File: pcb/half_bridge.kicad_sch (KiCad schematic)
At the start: 15 parts, among them Q1 IKW40N120H3, Q2 IKW40N120H3, U1 UCC21550BDWK

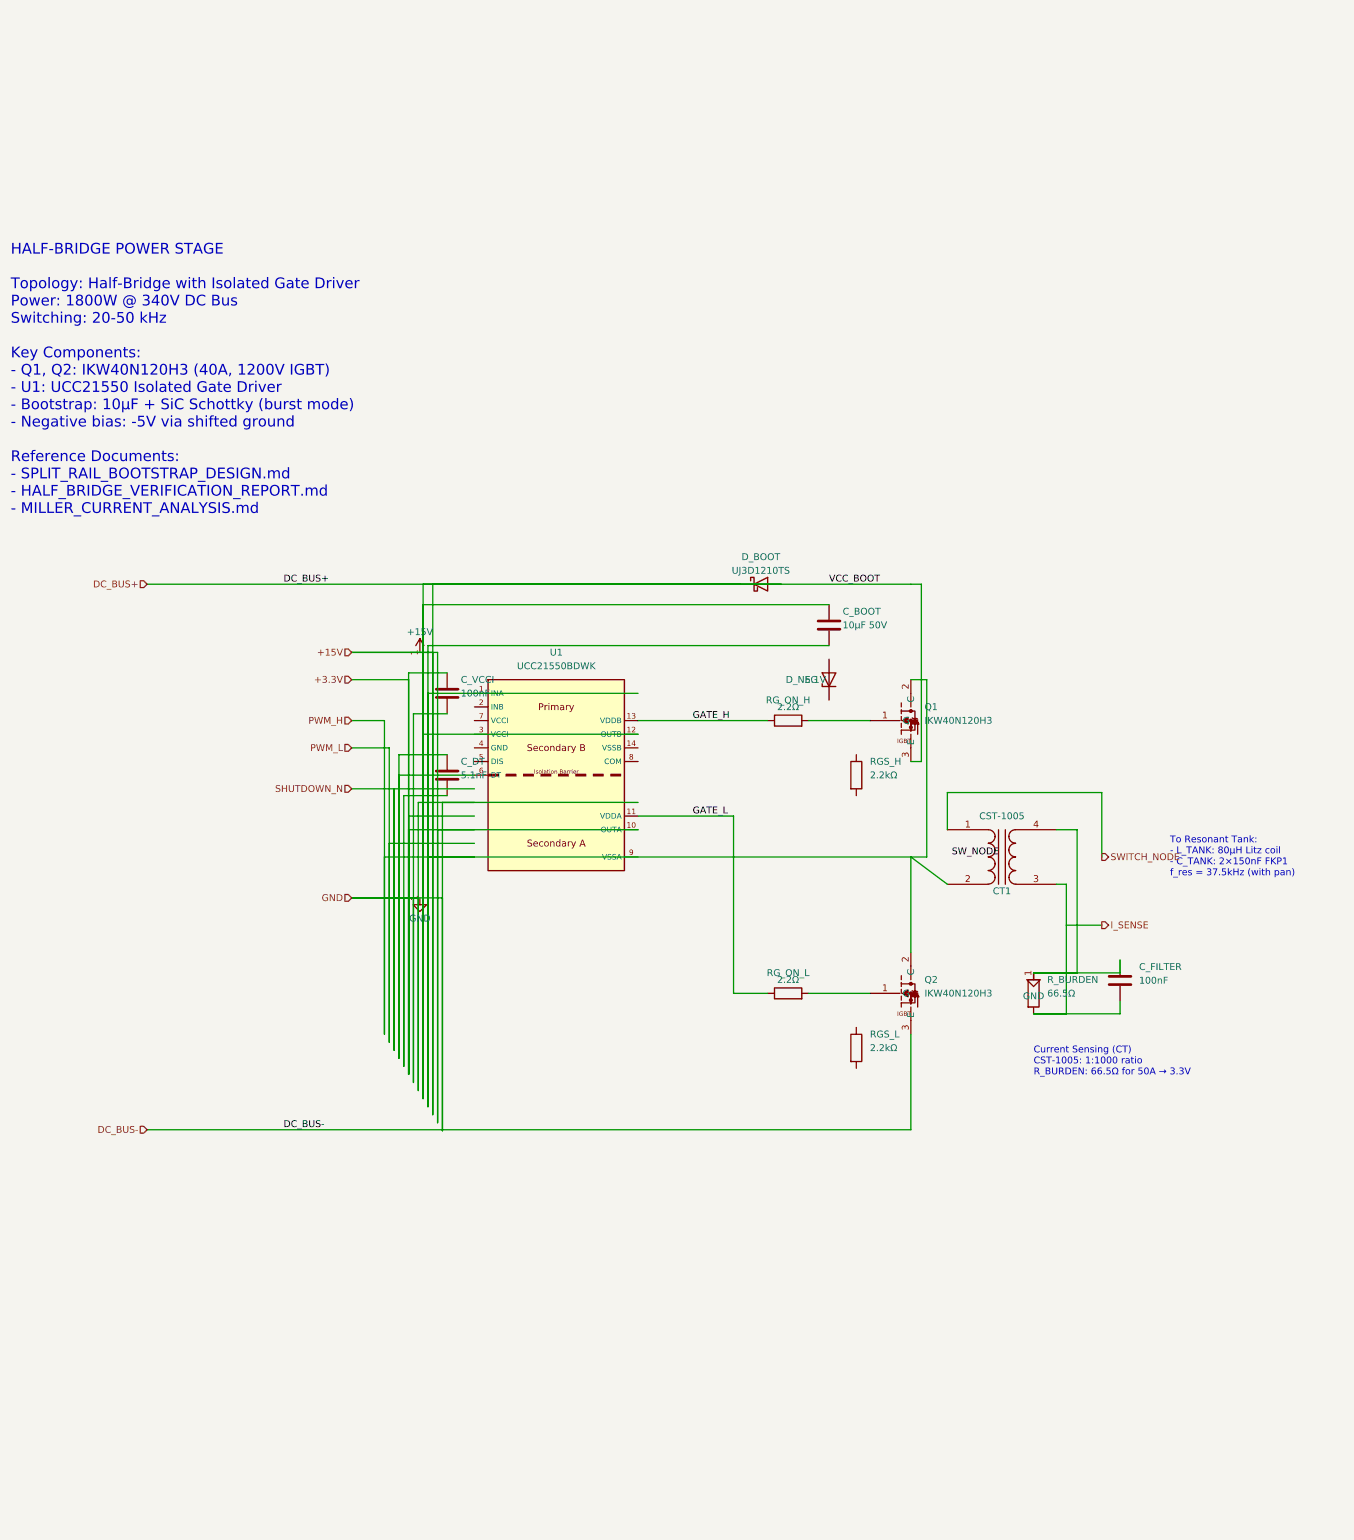
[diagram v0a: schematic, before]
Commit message: feat: generate KiCad schematics from atopile netlist
scripts/gen_schematics.py generates all 7 hierarchical KiCad schematic
files (root + 6 sub-sheets) from elec/build/default.net:

- Synthesizes box symbols from netlist libpart pin counts
- Pure label-per-pin connectivity (no wires)
- Hierarchical labels for inter-sheet nets
- Deterministic UUIDs from atopile tstamps
- Built-in oracle verifies connectivity partition isomorphism
- No-connect markers on intentionally-unconnected pins

Oracle: ORACLE PASS — 346 pin assignments, 73 multi-node nets,
connectivity partitions isomorphic.

Integrated into Makefile via 'make schematics' target.
Manifest entry added per repo convention.
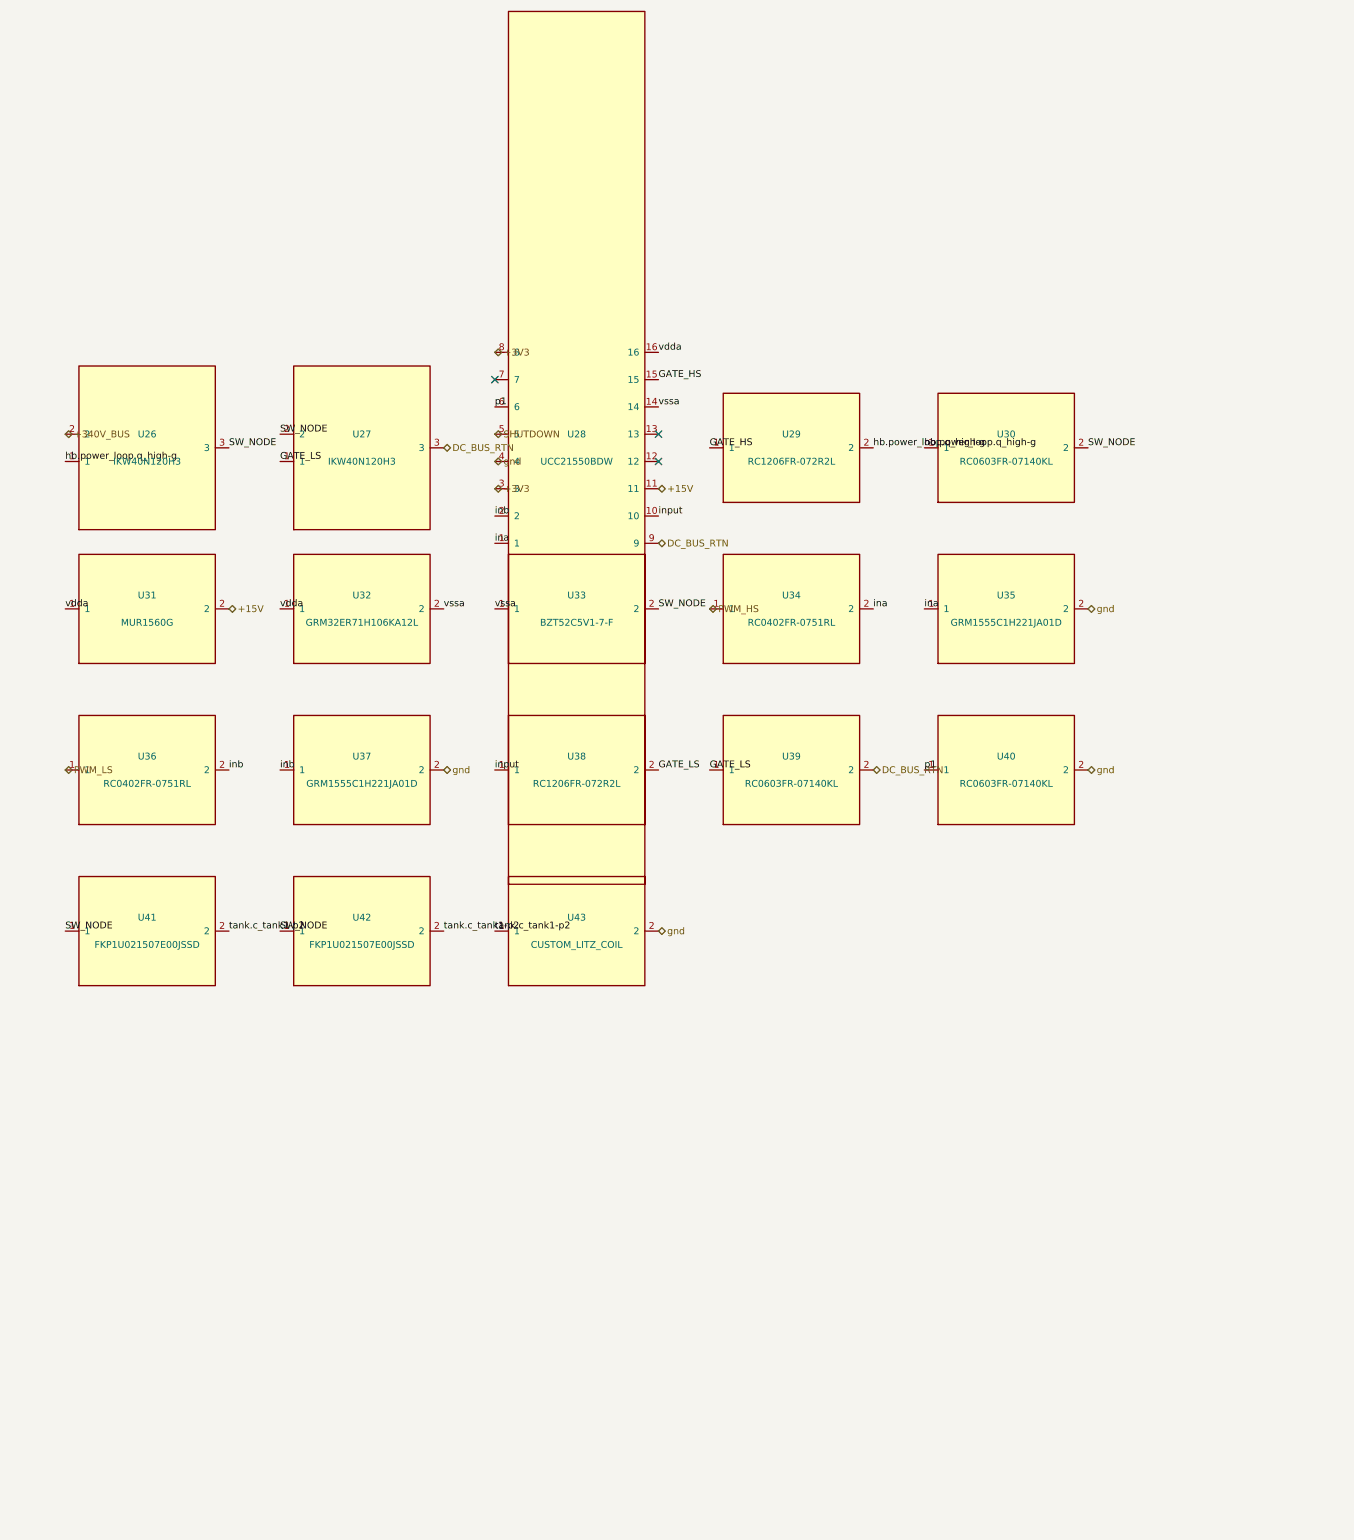
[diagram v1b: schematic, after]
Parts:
- removed CT1: CST-1005, temper:CST-1005, symbol Device:Transformer_1P_1S
- removed C_BOOT: 10µF 50V, Capacitor_SMD:C_1210_3225Metric, symbol Device:C
- removed C_DT: 5.1nF, Capacitor_SMD:C_0603_1608Metric, symbol Device:C
- removed C_FILTER, C_VCCI: 100nF, Capacitor_SMD:C_0603_1608Metric, symbol Device:C
- removed D_BOOT: UJ3D1210TS, Package_TO_SOT_THT:TO-220-2_Vertical, symbol Device:D_Schottky
- removed D_NEG: 5.1V, Diode_SMD:D_SOD-123, symbol Device:D_Zener
- removed Q1, Q2: IKW40N120H3, Package_TO_SOT_THT:TO-247-3_Vertical, symbol IKW40N120H3:IKW40N120H3
- removed RGS_H, RGS_L: 2.2kΩ, Resistor_SMD:R_0603_1608Metric, symbol Device:R
- removed RG_ON_H, RG_ON_L: 2.2Ω, Resistor_SMD:R_1206_3216Metric, symbol Device:R
- removed R_BURDEN: 66.5Ω, Resistor_SMD:R_1206_3216Metric, symbol Device:R
- removed U1: UCC21550BDWK, Package_SO:SOIC-16W_7.5x10.3mm_P1.27mm, symbol UCC21550:UCC21550DWK
- added U26, U27: IKW40N120H3, Package_TO_SOT_THT:TO-247-3_Vertical, symbol IKW40N120H3
- added U28: UCC21550BDW, lib:SOIC16W_Isolated, symbol UCC21550BDW
- added U29, U38: RC1206FR-072R2L, Resistor_SMD:R_1206_3216Metric, symbol RC1206FR-072R2L
- added U30, U39, U40: RC0603FR-07140KL, Resistor_SMD:R_0603_1608Metric, symbol RC0603FR-07140KL
- added U31: MUR1560G, Package_TO_SOT_THT:TO-220-2_Vertical, symbol MUR1560G
- added U32: GRM32ER71H106KA12L, Capacitor_SMD:C_1210_3225Metric, symbol GRM32ER71H106KA12L
- added U33: BZT52C5V1-7-F, Diode_SMD:D_SOD-123, symbol BZT52C5V1-7-F
- added U34, U36: RC0402FR-0751RL, Resistor_SMD:R_0402_1005Metric, symbol RC0402FR-0751RL
- added U35, U37: GRM1555C1H221JA01D, Capacitor_SMD:C_0402_1005Metric, symbol GRM1555C1H221JA01D
- added U41, U42: FKP1U021507E00JSSD, Capacitor_THT:C_Rect_L31.5mm_W13.0mm_P27.50mm_MKS4, symbol FKP1U021507E00JSSD
- added U43: CUSTOM_LITZ_COIL, lib:LitzPad_15A, symbol CUSTOM_LITZ_COIL
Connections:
- net +15V: now also U28.11, U31.2
- net SW_NODE: now also U26.3, U27.2, U30.2, U33.2, U41.1, U42.1
- new net +340V_BUS: U26.2
- new net +3V3: U28.3, U28.8
- new net DC_BUS_RTN: U27.3, U28.9, U39.2
- new net GATE_HS: U28.15, U29.1
- new net GATE_LS: U27.1, U38.2, U39.1
- new net PWM_HS: U34.1
- new net PWM_LS: U36.1
- new net SHUTDOWN: U28.5
- new net gnd: U28.4, U35.2, U37.2, U40.2, U43.2
- new net hb.power_loop.q_high-g: U26.1, U29.2, U30.1
- new net ina: U28.1, U34.2, U35.1
- new net inb: U28.2, U36.2, U37.1
- new net input: U28.10, U38.1
- new net p1: U28.6, U40.1
- new net tank.c_tank1-p2: U41.2, U42.2, U43.1
- new net vdda: U28.16, U31.1, U32.1
- new net vssa: U28.14, U32.2, U33.1
- no-connect marks 0 -> 3
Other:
- note removed: "Current Sensing (CT) CST-1005: 1:1000 ratio R_BURDEN: 66.5Ω for 50A → 3.3V"
- note removed: "HALF-BRIDGE POWER STAGE Topology: Half-Bridge with Isolated Gate Driver Power: 1800W @ 340V DC Bus Switching: 20-50 kHz Key Components: - Q1, Q2: IKW40N120H3 (40A, 1200V IGBT) - U1: UCC21550 Isolated Gate Driver - Bootstrap: 10µF + SiC Schottky (burst mode) - Negative bias: -5V via shifted ground Reference Documents: - SPLIT_RAIL_BOOTSTRAP_DESIGN.md - HALF_BRIDGE_VERIFICATION_REPORT.md - MILLER_C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"
- note removed: "To Resonant Tank: - L_TANK: 80µH Litz coil - C_TANK: 2×150nF FKP1 f_res = 37.5kHz (with pan)"
- title: Half Bridge Power Stage -> Half_Bridge

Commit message: chore: regenerate schematics from atopile netlist (#228)
Generated from elec/build/default.net via gen_schematics.py.
Adds 23 new components from discharge (17), aux_supply (4), and
thermal (2) modules that were previously un-mapped and absent.
Root sheet layout re-stacked with dynamic spacing.
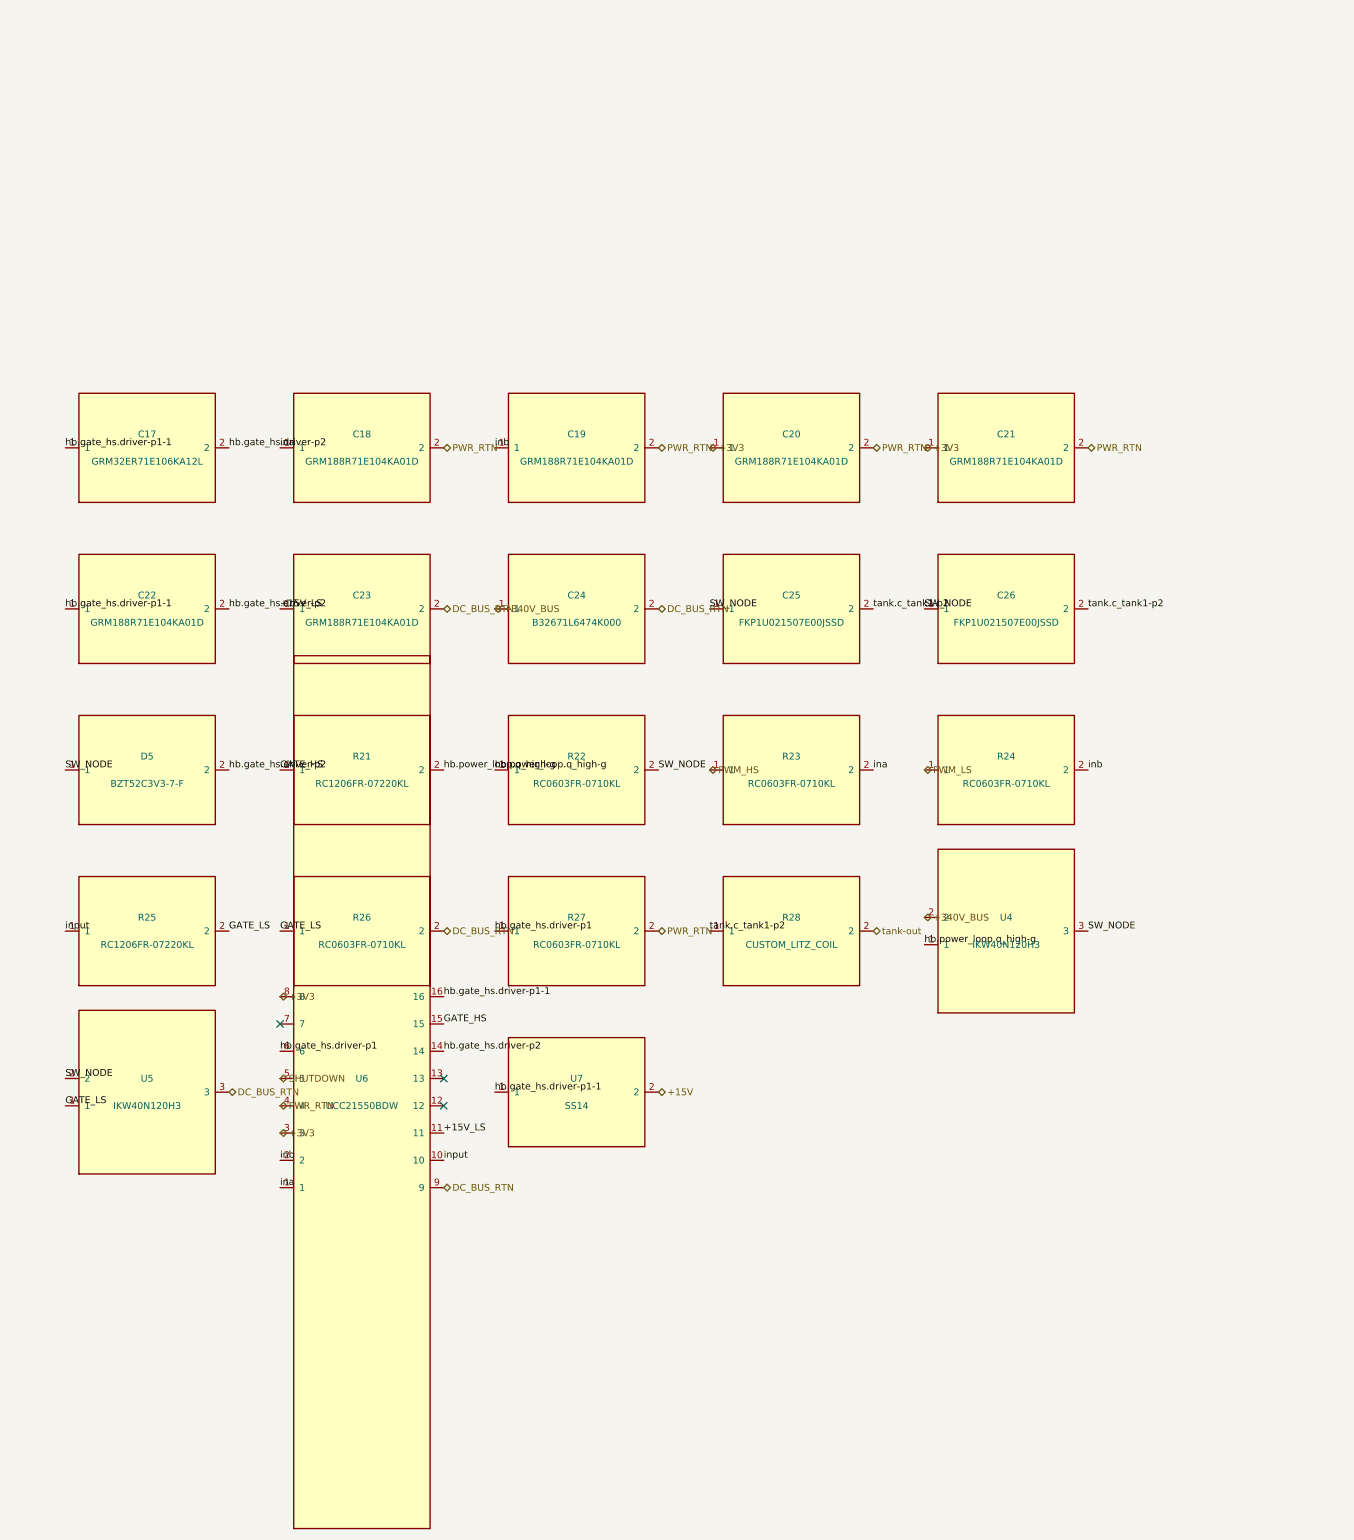
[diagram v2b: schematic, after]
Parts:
- added C20, C21, C22, C23: GRM188R71E104KA01D, Capacitor_SMD:C_0603_1608Metric, symbol GRM188R71E104KA01D
- added C24: B32671L6474K000, Capacitor_THT:C_Rect_L18.0mm_W11.0mm_P15.00mm_FKS3_FKP3, symbol B32671L6474K000
- C17: renamed from U32; value GRM32ER71H106KA12L -> GRM32ER71E106KA12L; symbol GRM32ER71H106KA12L -> GRM32ER71E106KA12L
- C18: renamed from U35; value GRM1555C1H221JA01D -> GRM188R71E104KA01D; footprint Capacitor_SMD:C_0402_1005Metric -> Capacitor_SMD:C_0603_1608Metric; symbol GRM1555C1H221JA01D -> GRM188R71E104KA01D
- C19: renamed from U37; value GRM1555C1H221JA01D -> GRM188R71E104KA01D; footprint Capacitor_SMD:C_0402_1005Metric -> Capacitor_SMD:C_0603_1608Metric; symbol GRM1555C1H221JA01D -> GRM188R71E104KA01D
- D5: renamed from U33; value BZT52C5V1-7-F -> BZT52C3V3-7-F; symbol BZT52C5V1-7-F -> BZT52C3V3-7-F
- R21: renamed from U29; value RC1206FR-072R2L -> RC1206FR-07220KL; symbol RC1206FR-072R2L -> RC1206FR-07220KL
- R22: renamed from U30; value RC0603FR-07140KL -> RC0603FR-0710KL; symbol RC0603FR-07140KL -> RC0603FR-0710KL
- R23: renamed from U34; value RC0402FR-0751RL -> RC0603FR-0710KL; footprint Resistor_SMD:R_0402_1005Metric -> Resistor_SMD:R_0603_1608Metric; symbol RC0402FR-0751RL -> RC0603FR-0710KL
- R24: renamed from U36; value RC0402FR-0751RL -> RC0603FR-0710KL; footprint Resistor_SMD:R_0402_1005Metric -> Resistor_SMD:R_0603_1608Metric; symbol RC0402FR-0751RL -> RC0603FR-0710KL
- R25: renamed from U38; value RC1206FR-072R2L -> RC1206FR-07220KL; symbol RC1206FR-072R2L -> RC1206FR-07220KL
- R26: renamed from U39; value RC0603FR-07140KL -> RC0603FR-0710KL; symbol RC0603FR-07140KL -> RC0603FR-0710KL
- R27: renamed from U40; value RC0603FR-07140KL -> RC0603FR-0710KL; symbol RC0603FR-07140KL -> RC0603FR-0710KL
- U7: renamed from U31; value MUR1560G -> SS14; footprint Package_TO_SOT_THT:TO-220-2_Vertical -> Diode_SMD:D_SMA; symbol MUR1560G -> SS14
- renumbered U41 to C25, U42 to C26, U43 to R28, U26 to U4, U27 to U5, U28 to U6
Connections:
- net +15V: no longer U6.11
- net +340V_BUS: now also C24.1
- net +3V3: now also C20.1, C21.1
- net DC_BUS_RTN: now also C23.2, C24.2
- net SW_NODE: now also D5.1; no longer D5.2
- net gnd renamed PWR_RTN
- net PWR_RTN: now also C20.2, C21.2; no longer R28.2
- net p1 renamed hb.gate_hs.driver-p1
- net vdda renamed hb.gate_hs.driver-p1-1
- net hb.gate_hs.driver-p1-1: now also C22.1
- net vssa renamed hb.gate_hs.driver-p2
- net hb.gate_hs.driver-p2: now also D5.2, C22.2; no longer D5.1
- new net +15V_LS: C23.1, U6.11
- new net tank-out: R28.2
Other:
- moved on the sheet: C17, C18, C19, C25, C26, D5, R21, R22, R23, R24, R25, R26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
